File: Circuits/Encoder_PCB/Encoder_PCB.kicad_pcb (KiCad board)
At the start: 2 copper layers, 14.3 x 15.8 mm, 7 parts, among them IC1 iC-PX2604, J1 Conn_01x04_Socket

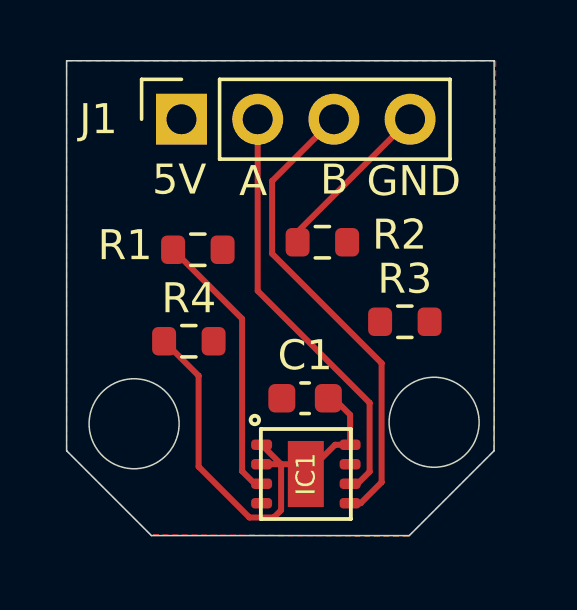
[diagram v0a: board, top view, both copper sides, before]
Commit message: Encoder PCB done, with step file
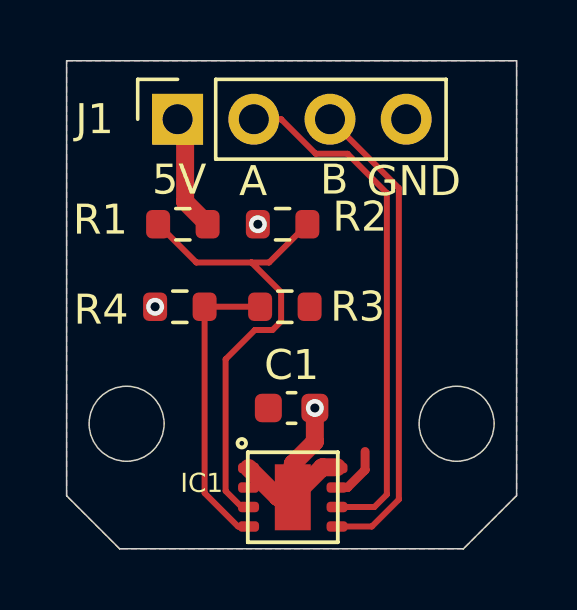
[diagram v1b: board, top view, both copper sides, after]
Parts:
- moved R3 4.03 mm to (138.1, 90.2)
- moved R2 1.45 mm to (138.0, 87.5)
- moved R4 1.19 mm to (134.6, 90.2)
- moved R1 0.99 mm to (134.7, 87.5)
- moved IC1 0.89 mm to (138.3, 96.6)
- moved C1 0.56 mm to (138.3, 93.6)
- moved J1 0.13 mm to (134.5, 84.0)
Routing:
- net GND: track 21.8 -> 7.06 mm, vias 0 -> 3
- net Net-(IC1-SEL2): track 0.00 -> 9.99 mm
- net Net-(IC1-SEL1): track 9.16 -> 16.2 mm
- net +5V: track 0.00 -> 5.71 mm
- net /CH-A: track 14.1 -> 17.3 mm
- added copper zone on B.Cu, net GND
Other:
- board size 14.3 x 15.8 mm -> 15 x 16.3 mm
